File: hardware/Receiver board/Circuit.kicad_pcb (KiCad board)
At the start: 2 copper layers, 31.5 x 35 mm, 8 parts, among them U1 PAM8403D

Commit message: Made Schematic for Reciever Board more Readable
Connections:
- U1 pad 12: +5V -> unconnected-(U1-~{SHDN}-Pad12)
- U1 pad 5: +5V -> unconnected-(U1-~{MUTE}-Pad5)
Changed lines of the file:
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@@
 	(net 9 "unconnected-(U1-ROUT--Pad14)")
 	(net 10 "unconnected-(U1-NC-Pad9)")
+	(net 11 "unconnected-(U1-~{SHDN}-Pad12)")
+	(net 12 "unconnected-(U1-~{MUTE}-Pad5)")
 	(footprint "Capacitor_THT:C_Disc_D3.0mm_W1.6mm_P2.50mm"
 		(layer "F.Cu")
@@
 			(layers "F.Cu" "F.Mask" "F.Paste")
 			(roundrect_rratio 0.25)
-			(net 5 "+5V")
+			(net 12 "unconnected-(U1-~{MUTE}-Pad5)")
 			(pinfunction "~{MUTE}")
-			(pintype "input")
+			(pintype "input+no_connect")
 		)
 		(pad "6" smd roundrect
@@
 			(layers "F.Cu" "F.Mask" "F.Paste")
 			(roundrect_rratio 0.25)
-			(net 5 "+5V")
+			(net 11 "unconnected-(U1-~{SHDN}-Pad12)")
 			(pinfunction "~{SHDN}")
-			(pintype "input")
+			(pintype "input+no_connect")
 		)
 		(pad "13" smd roundrect

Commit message: Updated Reciever Board
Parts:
- moved C3 17.0 mm to (182.0, 111.0)
- moved D1 9.61 mm to (205.0, 110.5), turned to 180 degrees
- moved C1 5.59 mm to (195.5, 111.5)
- moved C5 3.81 mm to (184.8, 105.5), turned to -90 degrees
- moved LS1 2.50 mm to (184.5, 98.5)
- moved C4 2.42 mm to (203.5, 103.5)
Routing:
- net Net-(U1-VREF): track 35.8 -> 5.86 mm
- net Net-(C3-Pad2): track 14.0 -> 32.4 mm
- net Net-(U1-INL): track 25.2 -> 11.8 mm
- net GND: track 81.4 -> 90.4 mm
- net Net-(U1-LOUT-): track 6.60 -> 7.27 mm
- net Net-(U1-LOUT+): track 6.60 -> 7.27 mm
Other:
- board size 31.5 x 35 mm -> 34 x 35 mm

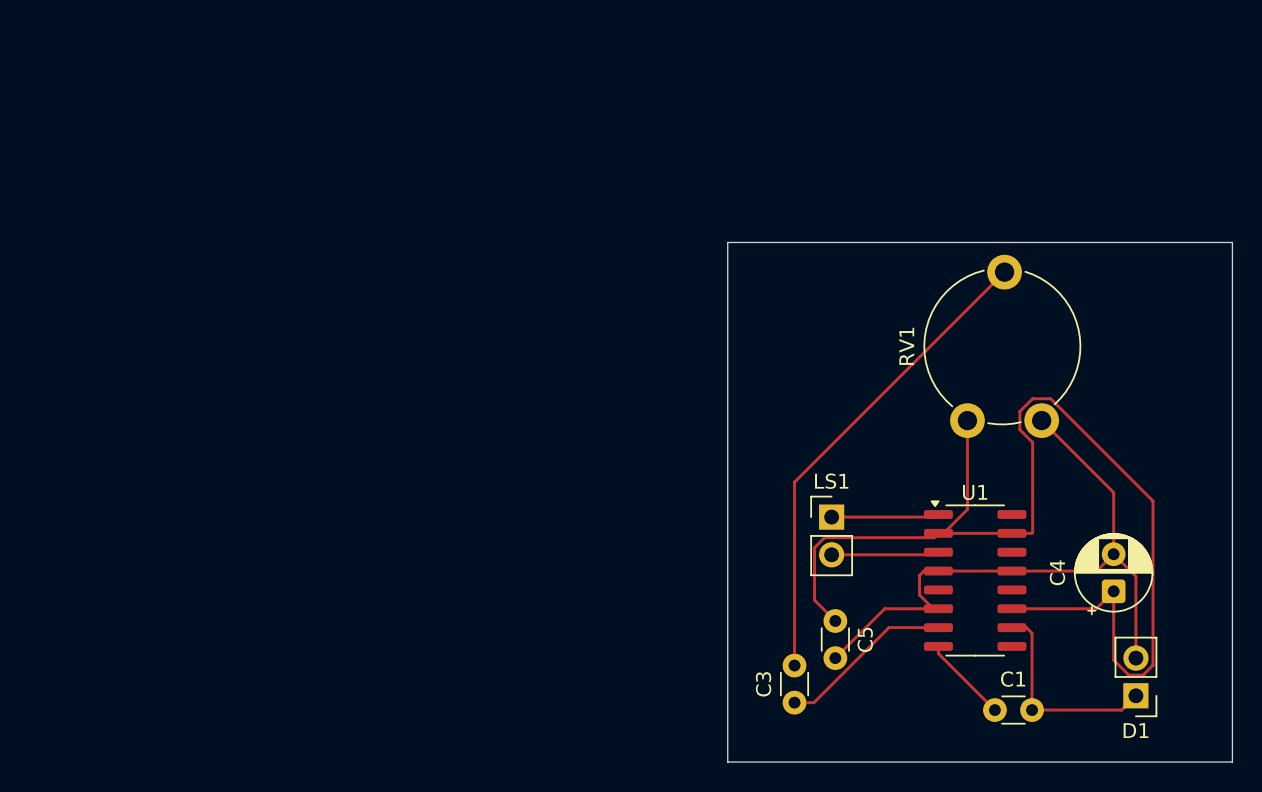
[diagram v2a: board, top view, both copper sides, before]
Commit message: Updated Schematic for Receiver: TIA with virtual ground for Op-Amps for handling negative half of the signal
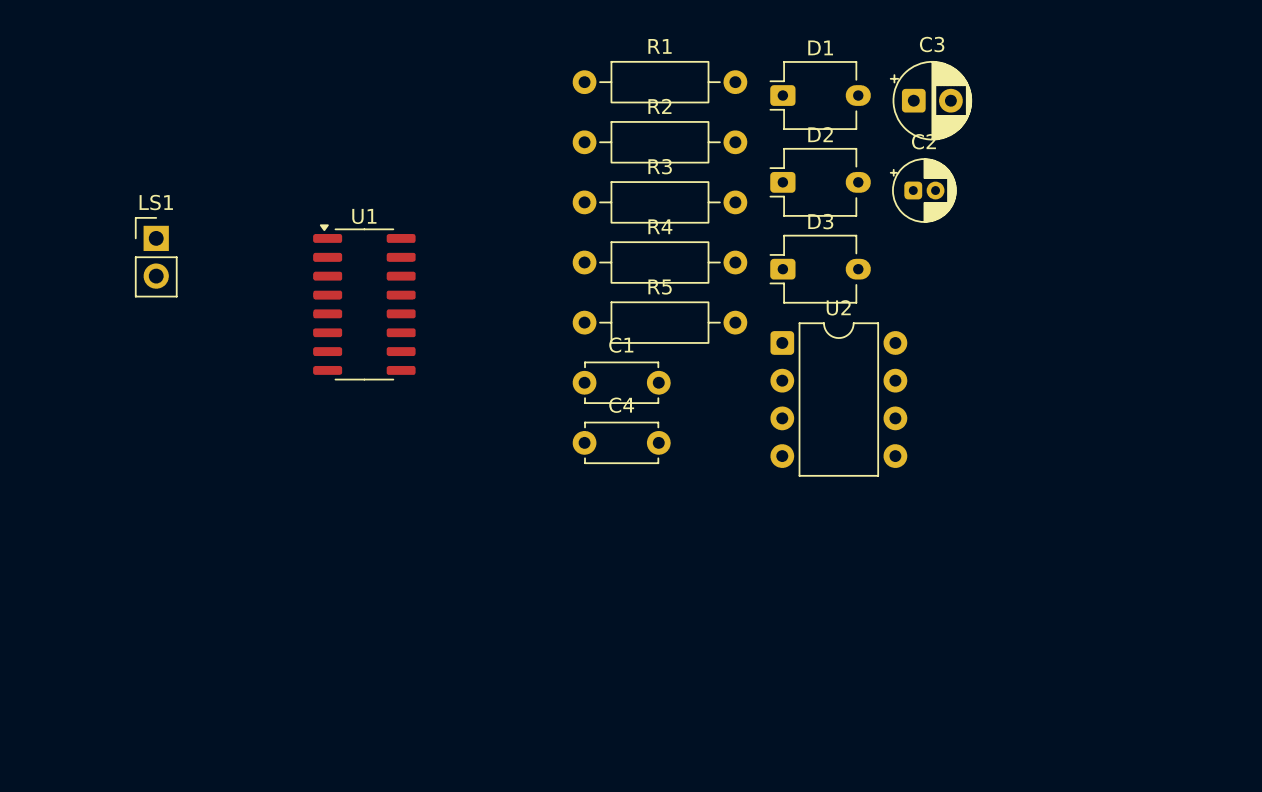
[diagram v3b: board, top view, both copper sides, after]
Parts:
- removed C5: 0.1uF, Capacitor_THT:C_Disc_D3.0mm_W1.6mm_P2.50mm
- removed RV1: 100k, Potentiometer_THT:Potentiometer_Piher_PT-10-V10_Vertical
- added C2: 1uF, Capacitor_THT:CP_Radial_D4.0mm_P1.50mm, F.Cu at (190.0, 76.5)
- added D2: BPW34, OptoDevice:Osram_DIL2_4.3x4.65mm_P5.08mm, F.Cu at (181.2, 76.0)
- added D3: BPW34, OptoDevice:Osram_DIL2_4.3x4.65mm_P5.08mm, F.Cu at (181.2, 81.8)
- added R1: 10k, Resistor_THT:R_Axial_DIN0207_L6.3mm_D2.5mm_P10.16mm_Horizontal, F.Cu at (167.9, 69.2)
- added R2: 10k, Resistor_THT:R_Axial_DIN0207_L6.3mm_D2.5mm_P10.16mm_Horizontal, F.Cu at (167.9, 73.2)
- added R3: 5.1k, Resistor_THT:R_Axial_DIN0207_L6.3mm_D2.5mm_P10.16mm_Horizontal, F.Cu at (167.9, 77.3)
- added R4: 10k, Resistor_THT:R_Axial_DIN0207_L6.3mm_D2.5mm_P10.16mm_Horizontal, F.Cu at (167.9, 81.3)
- added R5: 10k, Resistor_THT:R_Axial_DIN0207_L6.3mm_D2.5mm_P10.16mm_Horizontal, F.Cu at (167.9, 85.4)
- added U2: LM358, Package_DIP:DIP-8_W7.62mm, F.Cu at (181.2, 86.8)
- C1: footprint Capacitor_THT:C_Disc_D3.0mm_W1.6mm_P2.50mm -> Capacitor_THT:C_Disc_D4.7mm_W2.5mm_P5.00mm
- C3: value 1uF -> 20uF; footprint Capacitor_THT:C_Disc_D3.0mm_W1.6mm_P2.50mm -> Capacitor_THT:CP_Radial_D5.0mm_P2.50mm
- C4: value 10uF -> 0.1uF; footprint Capacitor_THT:CP_Radial_D5.0mm_P2.50mm -> Capacitor_THT:C_Disc_D4.7mm_W2.5mm_P5.00mm
- D1: value D -> BPW34; footprint Connector_PinHeader_2.54mm:PinHeader_1x02_P2.54mm_Vertical -> OptoDevice:Osram_DIL2_4.3x4.65mm_P5.08mm
- moved LS1 49.2 mm to (139.0, 79.7)
- moved D1 46.9 mm to (181.2, 70.1), turned to 0 degrees
- moved U1 45.2 mm to (153.0, 84.2)
- moved C3 41.3 mm to (190.0, 70.5), turned to 0 degrees
- moved C4 37.0 mm to (167.9, 93.5), turned to 0 degrees
- moved C1 35.4 mm to (167.9, 89.5)
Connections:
- C3 pad 1: Net-(U1-INL) -> +5V
- C3 pad 2: Net-(C3-Pad2) -> GND
- C4 pad 1: GND -> +5V
- C4 pad 2: +5V -> GND
- D1 pad 1: GND -> Net-(D1-K)
- D1 pad 2: +5V -> GND
- U1 pad 12: unconnected-(U1-~{SHDN}-Pad12) -> +5V
- U1 pad 5: unconnected-(U1-~{MUTE}-Pad5) -> +5V
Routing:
- net GND: track 90.4 -> 0.00 mm
- net +5V: track 43.6 -> 0.00 mm
- net Net-(C3-Pad2): track 32.4 -> 0.00 mm
- net Net-(U1-INL): track 11.8 -> 0.00 mm
- net Net-(U1-LOUT-): track 7.27 -> 0.00 mm
- net Net-(U1-LOUT+): track 7.27 -> 0.00 mm
- net Net-(U1-VREF): track 5.86 -> 0.00 mm
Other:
- board outline removed

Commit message: Layout updated after the Schematic update
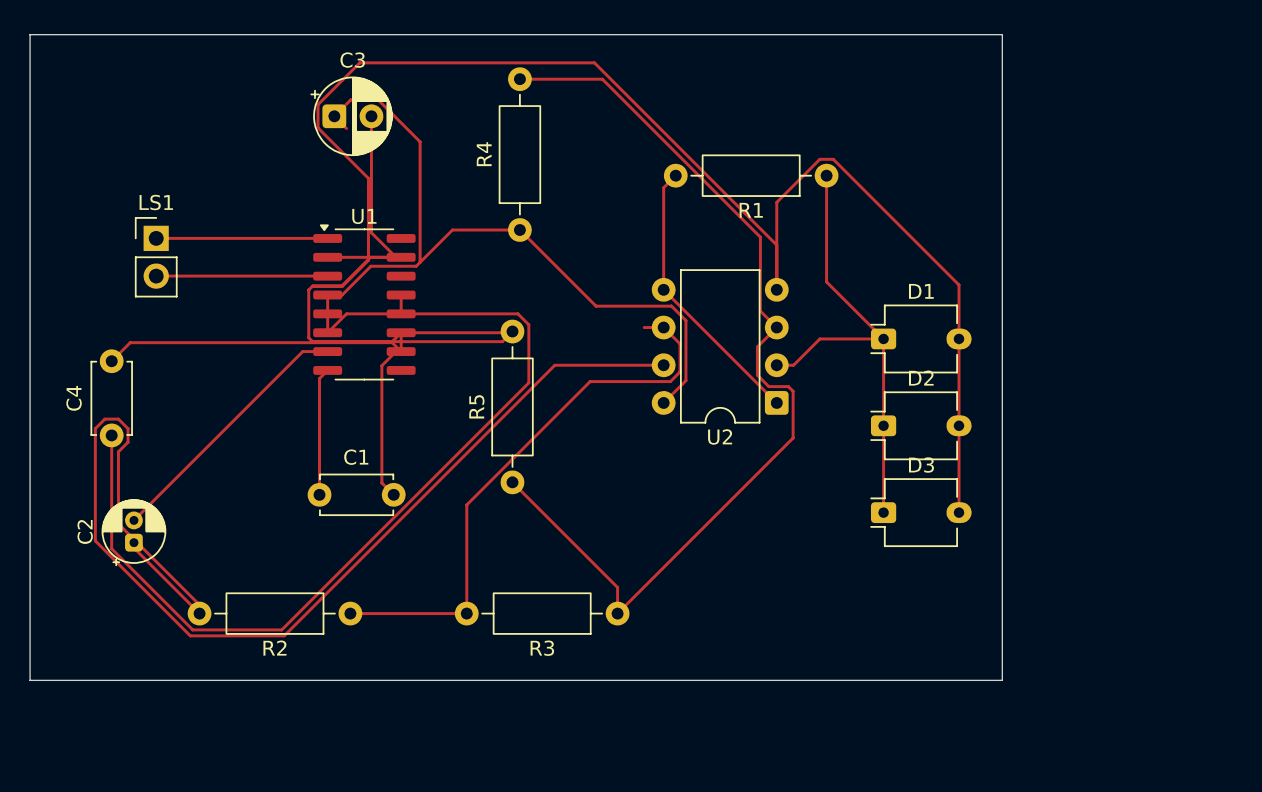
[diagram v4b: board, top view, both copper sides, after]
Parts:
- moved C2 57.6 mm to (137.5, 100.2), turned to 90 degrees
- moved C3 39.0 mm to (151.0, 71.5)
- moved R2 35.5 mm to (152.1, 105.0), turned to 180 degrees
- moved C4 31.9 mm to (136.0, 93.0), turned to 90 degrees
- moved R3 27.8 mm to (170.1, 105.0), turned to 180 degrees
- moved C1 19.4 mm to (150.0, 97.0)
- moved D1 17.7 mm to (188.0, 86.5)
- moved D3 17.7 mm to (188.0, 98.2)
- moved D2 17.7 mm to (188.0, 92.3)
- moved R1 17.5 mm to (184.2, 75.5), turned to 180 degrees
- moved R5 11.8 mm to (163.0, 96.2), turned to 90 degrees
- moved R4 4.87 mm to (163.5, 79.2), turned to 90 degrees
- moved U2 4.06 mm to (180.8, 90.8), turned to 180 degrees
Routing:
- net GND: track 0.00 -> 180.7 mm
- net +5V: track 0.00 -> 118.3 mm
- net Net-(C2-Pad1): track 0.00 -> 80.4 mm
- net Net-(U2A-+): track 0.00 -> 65.4 mm
- net Net-(U2B--): track 0.00 -> 38.0 mm
- net Net-(D1-K): track 0.00 -> 32.2 mm
- net Net-(U2B-+): track 0.00 -> 18.8 mm
- net Net-(U1-INL): track 0.00 -> 17.8 mm
- net Net-(U1-LOUT+): track 0.00 -> 11.6 mm
- net Net-(U1-LOUT-): track 0.00 -> 11.6 mm
- net Net-(U1-VREF): track 0.00 -> 8.61 mm
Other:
- board outline added: 65.5 x 43.5 mm
